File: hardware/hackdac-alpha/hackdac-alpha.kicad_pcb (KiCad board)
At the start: 4 copper layers, 120 x 75 mm, 203 parts, among them J1 VIDEO OUT, J10 HOLE, J11 HOLE, J12 HOLE, J2 TTL SYNC, J3 SYNC/VIDEO OUT, J4 I2C, J5 AUDIO OUT, J6 EXT POWER, J7 HOLE, J8 HOLE, J9 HOLE, P1 BANK2_AUX, P2 P22, P3 P28, P4 P20, Q1 2N7002, Q2 BC847, Q3 BC857, Q4 BC857, Q5 IRLML2244, U1 AD768, U10 PCM5102, U11 74LVC1G07, U12 TPS61170DRVR, U13 TPS63700DRCT, U2 MAX4104, U3 TLE2082, U4 MAX4104, U5 MCP47FEB22A1-E/ST, U6 74LVCH16T245, U7 74LVC1G125, U8 MCP1700T-3302E/MB, U9 TCA9517D, X1 ECS-5032MV-270-CN-TR

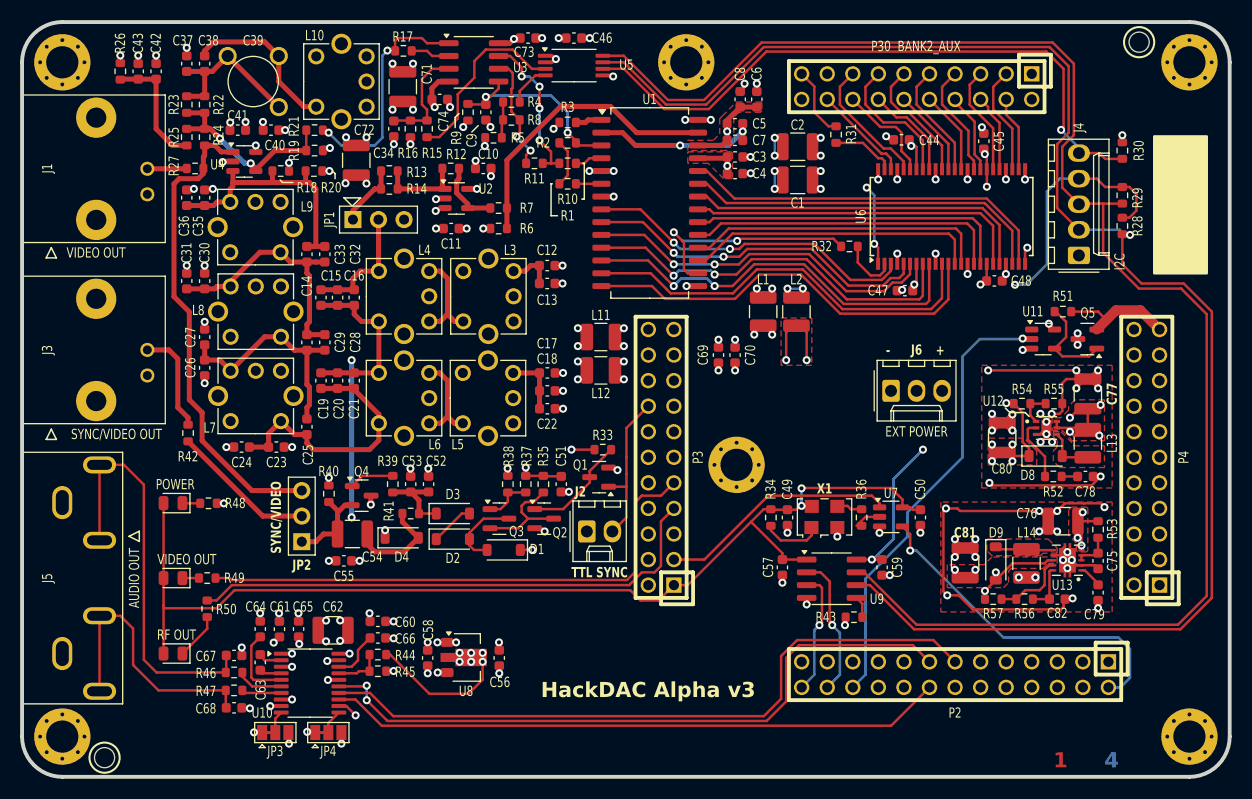
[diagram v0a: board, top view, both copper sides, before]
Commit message: Added configuration straps
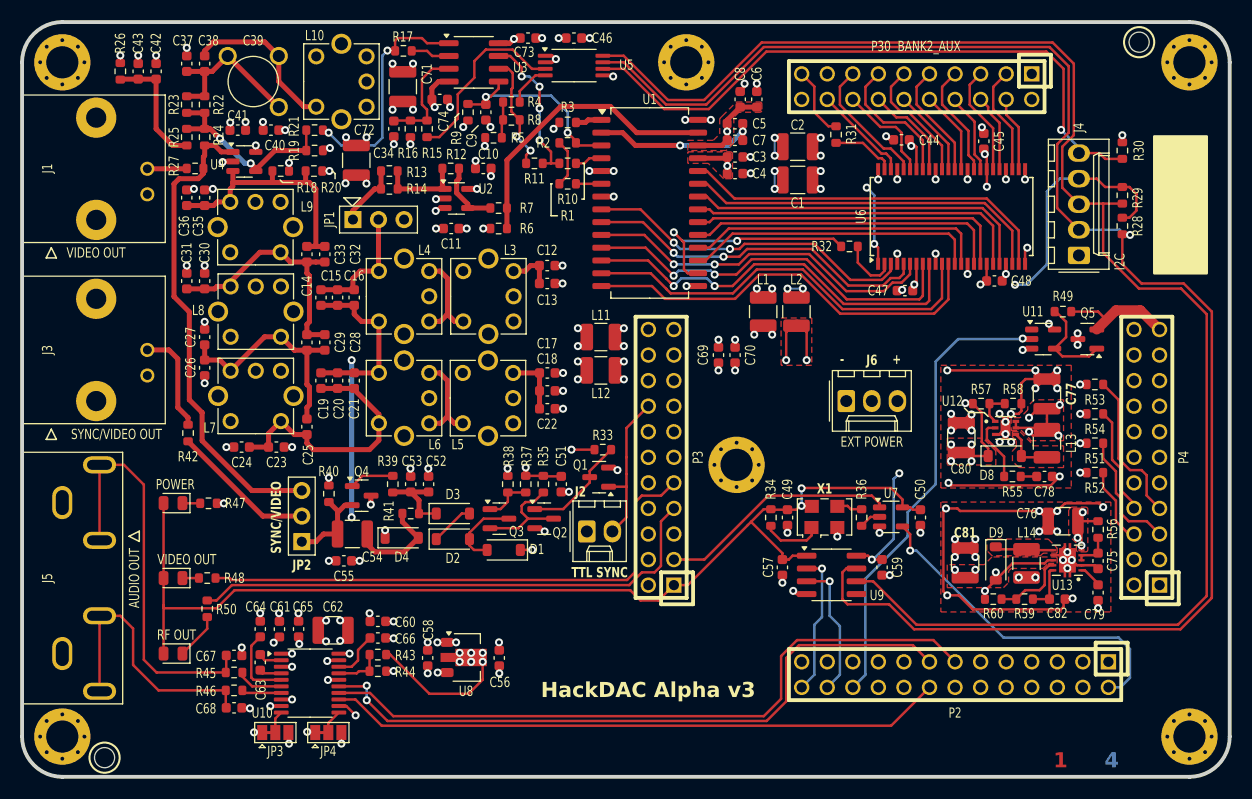
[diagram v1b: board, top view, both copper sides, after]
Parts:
- removed the R43 at (162.4, 122.9)
- added R51: NF, Resistor_SMD:R_0603_1608Metric, F.Cu at (186.3, 105.6)
- added R52: NF, Resistor_SMD:R_0603_1608Metric, F.Cu at (186.3, 108.5)
- added R53: NF, Resistor_SMD:R_0603_1608Metric, F.Cu at (186.3, 99.8)
- added R54: NF, Resistor_SMD:R_0603_1608Metric, F.Cu at (186.3, 102.7)
- moved J6 4.56 mm to (161.6, 101.4)
- moved C78 4.06 mm to (181.3, 108.9)
- moved C80 4.06 mm to (173.0, 105.0)
- moved R57 4.06 mm to (175.0, 101.7)
- moved R58 4.06 mm to (178.2, 101.7)
- moved C77 4.06 mm to (181.5, 100.7)
- moved D8 4.06 mm to (177.4, 106.9)
- moved L13 4.06 mm to (181.5, 105.6)
- moved R55 4.06 mm to (178.1, 108.9)
- moved U12 4.06 mm to (177.4, 104.1)
- moved U9 0.38 mm to (160.1, 118.7)
- renumbered R44 to R43, R45 to R44, R46 to R45, R47 to R46, R48 to R47, R49 to R48, R51 to R49, R52 to R55, R53 to R56, R54 to R57, R55 to R58, R56 to R59, R57 to R60
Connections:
- P4 pad 5: unconnected-(P4-Pin_5-Pad5) -> /power/CFG0
- P4 pad 6: unconnected-(P4-Pin_6-Pad6) -> /power/CFG1
- P4 pad 7: unconnected-(P4-Pin_7-Pad7) -> /power/CFG2
- P4 pad 8: unconnected-(P4-Pin_8-Pad8) -> /power/CFG3
- U9 pad 2: /audio/SDA -> /audio/SCL
- U9 pad 3: /audio/SCL -> /audio/SDA
- U9 pad 5: Net-(U9-EN) -> unconnected-(U9-EN-Pad5)
- U9 pad 6: DA_SCL -> DA_SDA
- U9 pad 7: DA_SDA -> DA_SCL
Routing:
- net /power/CFG2: track 0.00 -> 15.3 mm
- net /power/CFG0: track 0.00 -> 12.4 mm
- net +5V: track 168.1 -> 179.3 mm
- net /power/CFG3: track 0.00 -> 10.7 mm
- net GND: track 1137.0 -> 1145.8 mm, vias 144 -> 147
- net /power/CFG1: track 0.00 -> 7.67 mm
- net DA_SCL: track 155.6 -> 160.6 mm
- net -5V: track 70.3 -> 66.2 mm
- net Net-(U9-EN): track 2.16 -> 0.00 mm
- net /audio/SCL: track 12.5 -> 14.2 mm
- net PWR_EN: track 45.0 -> 46.3 mm
- net VIN: track 138.4 -> 137.5 mm
- net Net-(R36-Pad2): track 2.28 -> 1.77 mm

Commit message: V3 tid-ups
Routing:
- net +5V: track 179.3 -> 179.6 mm, vias 17 -> 16

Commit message: Final V3 board
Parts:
- J3: value SYNC/VIDEO OUT -> VIDEO/SYNC OUT
- JP2: value SYNC/VIDEO -> VIDEO/SYNC
- moved JP2 0.57 mm to (107.0, 115.2), turned to -90 degrees
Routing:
- net Net-(JP2-C): track 14.4 -> 16.1 mm, vias 0 -> 1
- net Net-(JP2-A): track 9.16 -> 9.66 mm

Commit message: Fixed a couple of incorrect component values
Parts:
- C28: value NF -> 270p
- C29: value 270p -> NF
- C62: value 10uF -> 10u
- L14: value 4u7 -> 5u6
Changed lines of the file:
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@@
 			)
 		)
-		(property "Value" "270p"
+		(property "Value" "NF"
 			(at 0 1.43 90)
 			(layer "F.Fab")
@@
 			)
 		)
-		(property "Value" "4u7"
+		(property "Value" "5u6"
 			(at 0 2.28 90)
 			(layer "F.Fab")
@@
 			)
 		)
-		(property "Value" "NF"
+		(property "Value" "270p"
 			(at 0 1.43 90)
 			(layer "F.Fab")
@@
 			)
 		)
-		(property "Value" "10uF"
+		(property "Value" "10u"
 			(at 0 2.3 0)
 			(layer "F.Fab")
